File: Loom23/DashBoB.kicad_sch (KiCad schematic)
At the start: 0 parts

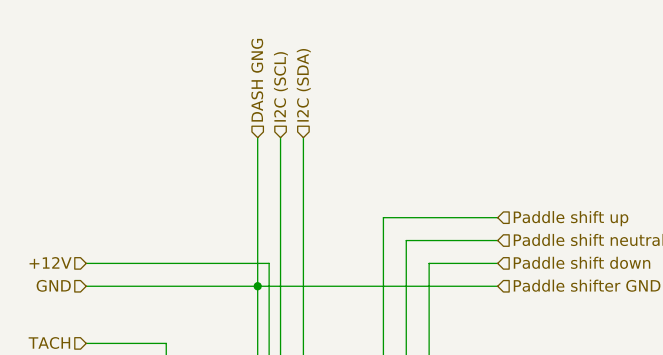
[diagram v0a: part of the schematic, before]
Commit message: Finished wire labels
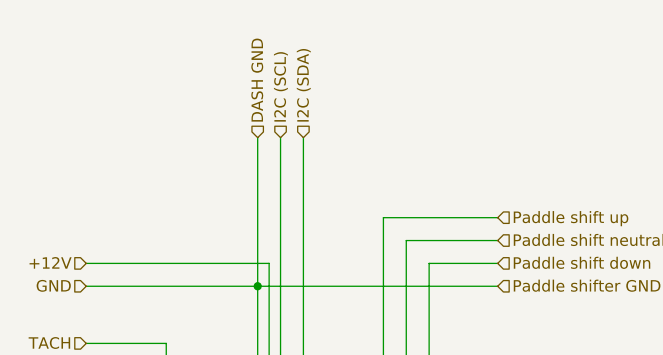
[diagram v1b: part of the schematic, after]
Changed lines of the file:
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@@
     (effects (font (size 1.27 1.27)) (justify left))
   )
-  (hierarchical_label "DASH GNG" (shape input) (at 146.05 72.39 90)
+  (hierarchical_label "DASH GND" (shape input) (at 146.05 72.39 90)
     (effects (font (size 1.27 1.27)) (justify left))
   )
